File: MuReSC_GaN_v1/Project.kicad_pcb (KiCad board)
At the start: 4 copper layers, 96.7 x 40 mm, 122 parts, among them IC1 STM32G474RET6, IC10 UCC12040DVE, IC11 LMG1020YFFR, IC12 LMG1020YFFR, IC13 LMG1020YFFR, IC14 LMG1020YFFR, IC2 TPSM5601R5HRDAR, IC3 ISO7720FQDQ1, IC4 ISO7720FQDQ1, IC5 ISO7720FQDQ1, IC6 ISO7720FQDQ1, IC7 UCC12040DVE, IC8 UCC12040DVE, IC9 UCC12040DVE, J1 Conn_01x05, J2 Conn_01x02, J3 Conn_01x01, J4 Conn_01x01, J5 Conn_01x01, P1 691214110002, P2 691214110002, Q1 GS61004B-TR, Q2 GS61004B-TR, Q3 GS61004B-TR, Q4 GS61004B-TR, Y1 NX3215SA-32.768K-STD-MUS-2, Y2 NX3225SA-24.000MHZ-STD-CSR-1

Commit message: update
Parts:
- added JP1: Jumper_2_Bridged, Connector_PinHeader_2.54mm:PinHeader_1x02_P2.54mm_Vertical, F.Cu at (56.3, 81.2)
- moved RS7 14.0 mm to (60.1, 88.9), turned to 180 degrees
- moved Z3 10.5 mm to (61.9, 86.6), turned to 180 degrees
- moved RS8 9.27 mm to (63.6, 88.9), turned to 180 degrees
- moved P1 3.96 mm to (68.6, 82.8)
- moved P2 1.20 mm to (85.0, 82.8)
- moved C3 1.20 mm to (83.3, 88.4)
- moved TPS3 0.70 mm to (77.7, 110.0)
- moved CIN2 0.63 mm to (52.4, 85.3)
- moved CIN1 0.55 mm to (55.4, 85.2)
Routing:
- net /ADC2_IN2: track 67.4 -> 56.0 mm
- net /COMP1_INP: track 24.0 -> 29.9 mm, vias 3 -> 2
- net /VDD48V: track 5.00 -> 9.62 mm, vias 28 -> 0
- net GND: track 329.7 -> 332.9 mm, vias 250 -> 270
- removed copper zone on In2.Cu, net /VDD48V

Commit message: up
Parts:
- turned RS3 to 0 degrees
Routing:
- net /S2: track 140.8 -> 173.4 mm
- net GND: track 332.9 -> 333.6 mm, vias 270 -> 269
- net /NRST: track 44.3 -> 44.9 mm

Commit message: Ultime_modifiche
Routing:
- net /VDD5V: track 36.1 -> 30.9 mm
- net /S2: track 173.4 -> 175.9 mm
- net /VDD3V3: track 19.7 -> 20.8 mm
- net /COMP1_INP: track 30.1 -> 29.2 mm
- net /STLINK_RX: track 19.7 -> 18.9 mm
- net GND: track 333.6 -> 333.0 mm
- net /VDDI4: track 25.1 -> 25.6 mm

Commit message: MuReSCC_V1_def
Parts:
- moved CTP3 4.57 mm to (46.3, 113.5)
- moved CTP1 2.07 mm to (46.5, 99.4), turned to -90 degrees
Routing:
- net GND: track 333.0 -> 335.6 mm

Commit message: footprint
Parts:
- CISOP1, CISOP2, CISOP3, CISOP4, CISOS1, CISOS2, CISOS3, CISOS4: value GRT155R70J105KE01D -> C0402C104K8RACTU
- CM1, CM10, CM2, CM3, CM4, CM6, CM7, CM9, CTP1, CTP2, CTP3, CTP4, CTS1, CTS2, CTS3, CTS4: value C0402C104K8RAC7867 -> C0402C104K8RACTU
- J1: footprint Connector_PinHeader_2.54mm:PinHeader_1x05_P2.54mm_Vertical -> SamacSys_Parts:PinHeader_1x05_P2.54mm_Horizontal
- J2, JP1: footprint Connector_PinHeader_2.54mm:PinHeader_1x02_P2.54mm_Vertical -> SamacSys_Parts:PinHeader_1x02_P2.54mm_Horizontal
- moved C3 1.44 mm to (83.0, 87.0)
- turned IC1 to -90 degrees
- turned J1 to -90 degrees
- turned J2 to 90 degrees
- turned JP1 to 0 degrees

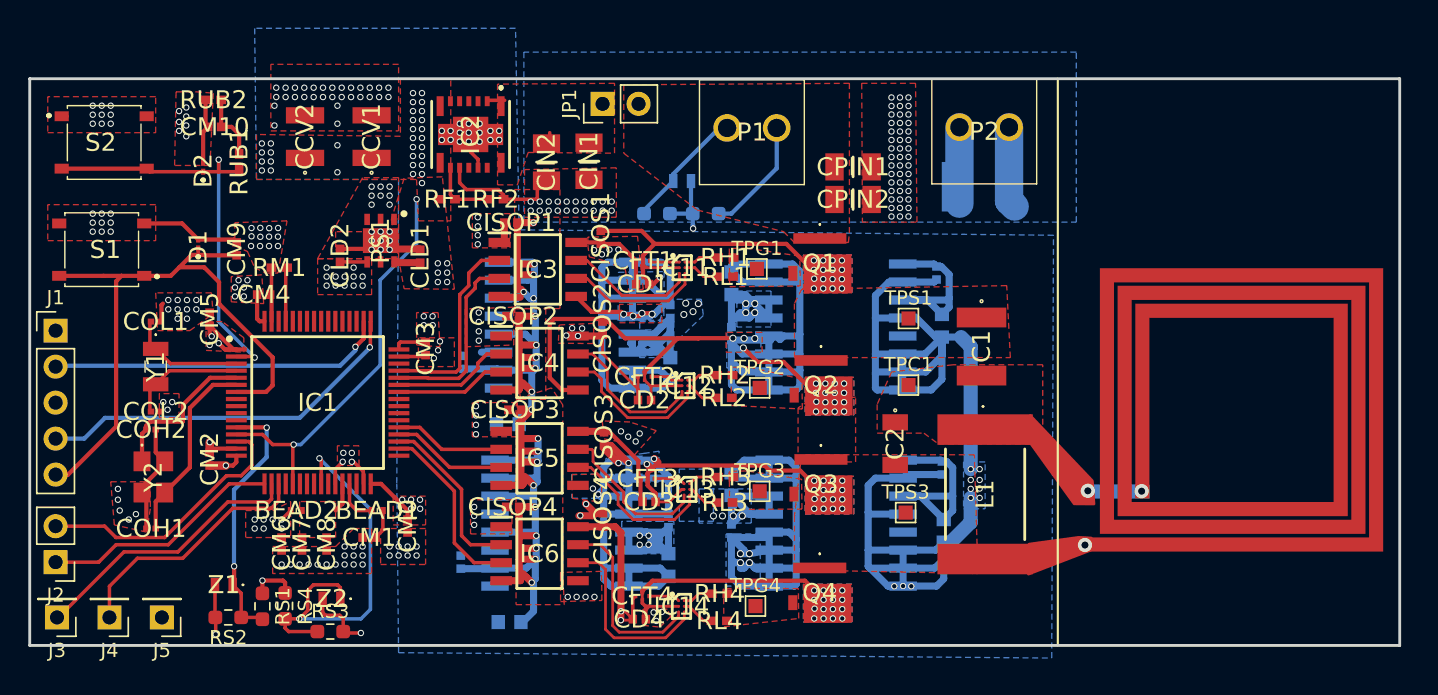
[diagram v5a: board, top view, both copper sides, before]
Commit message: footprint correction
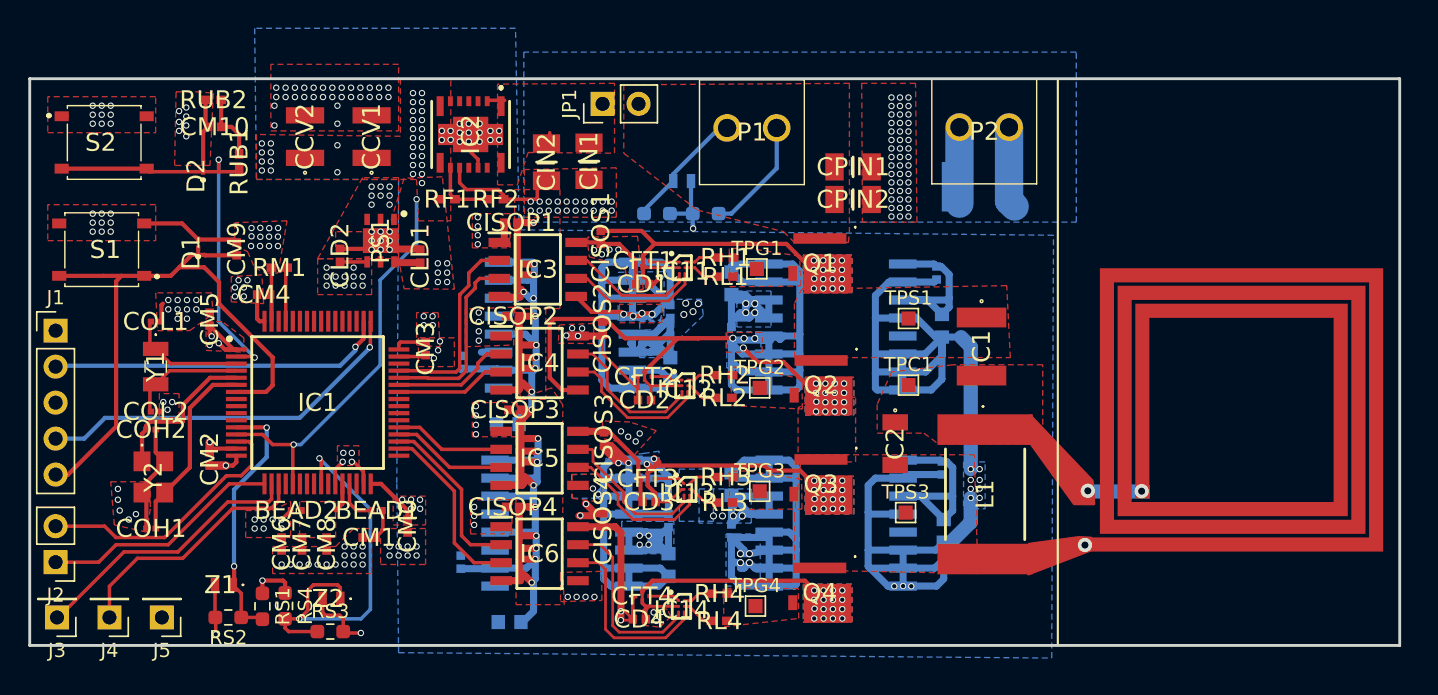
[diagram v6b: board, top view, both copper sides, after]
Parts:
- turned PS1 to 180 degrees

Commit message: MuReSC_GaN_V2
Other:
- outline, holes or cut-outs redrawn
- board text added: "Planar Custom Inductor Width = 1mm 3 Turn 4 Layer"

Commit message: Silkscrin
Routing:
- net /S2: track 175.9 -> 174.7 mm
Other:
- outline, holes or cut-outs redrawn
- board text added: "Designed in Bologna CERN-OHL-S v2"
- board text added: "Nenelina-board M. Guerrini and M. Villa"
- board text added: "Nenelina-board developed by Marco Guerrini and Marco Villa Bologna, december 2023 License: CERN-OHL-S v2"
- board text added: "Planar Custom Inductor Width = 1mm 3 Turn 4 Layer L = 220nH"
- board text removed: "Planar Custom Inductor Width = 1mm 3 Turn 4 Layer"
